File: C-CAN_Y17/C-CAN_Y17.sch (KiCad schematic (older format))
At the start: 18 parts, among them P1 CAN_Connector, P2 Sensor_Connector, P3 CAN_Terminate, SW1 SW_Push, U1 MCP2551-I/SN, U2 AP111750, U3 Cypress_5LP, Y1 Crystal

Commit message: Remove uneccesary junctions, add MX150 symbols
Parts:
- removed R2: 1k, Resistors_SMD:R_0805_HandSoldering, symbol R
- added P?: MX150_16, symbol MX150_16
- added P?: MX150_8, symbol MX150_8
- added R2: 1k, symbol R_Small
- P1: symbol CONN_02X04 -> CONN_02X04-RESCUE-C-CAN_Y17
- P2: symbol CONN_02X08 -> CONN_02X08-RESCUE-C-CAN_Y17
- U2: symbol AP111750 -> AP111750-RESCUE-C-CAN_Y17
- Y1: symbol Crystal -> Crystal-RESCUE-C-CAN_Y17
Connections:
- net +12V: now also P?.1 (P1), P?.4 (P7)
- net +5V: now also P?.1 (P1), P?.12, P?.4, P?.7, P?.9, R2.2
- net GND: now also P?.11, P?.14, P?.15, P?.16, P?.3, P?.5 (P2), P?.6, P?.8 (P8)
- net H1: now also P?.8
- net S1: now also P?.2
- net S2: now also P?.5
- net S3: now also P?.10
- net S4: now also P?.13
- net at SW1.1, U3.24 (RESET): now also R2.1
- new net CANH: P?.2 (P3), P?.3 (P5)
- new net CANL: P?.6 (P4), P?.7 (P6)

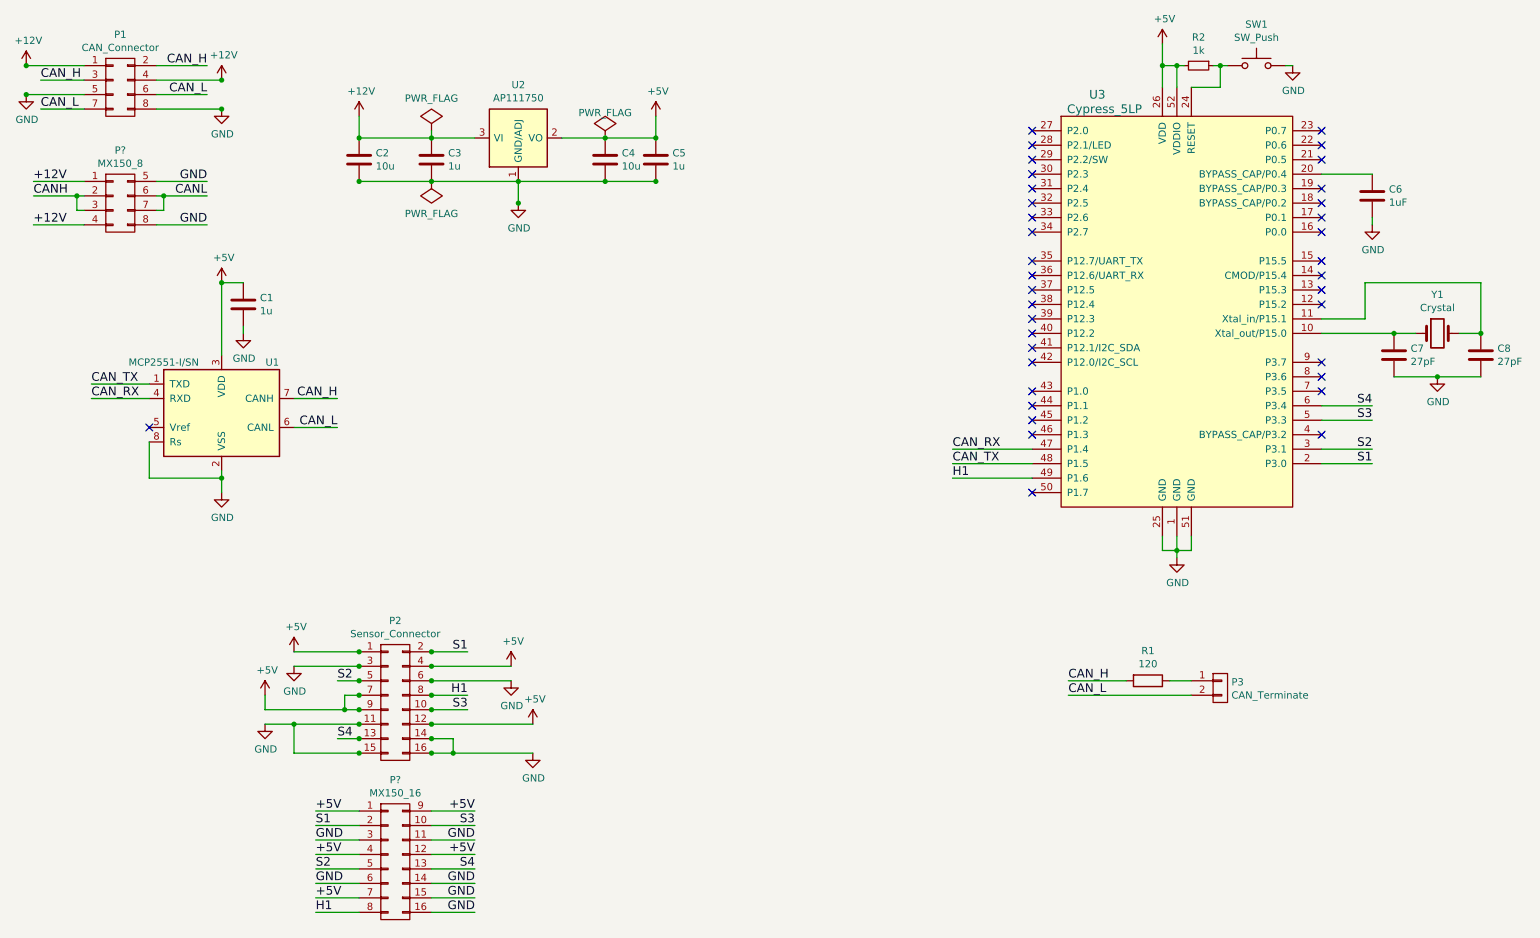
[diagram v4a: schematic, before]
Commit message: Fix AP1117 error, remove extraneous PWR_FLAG
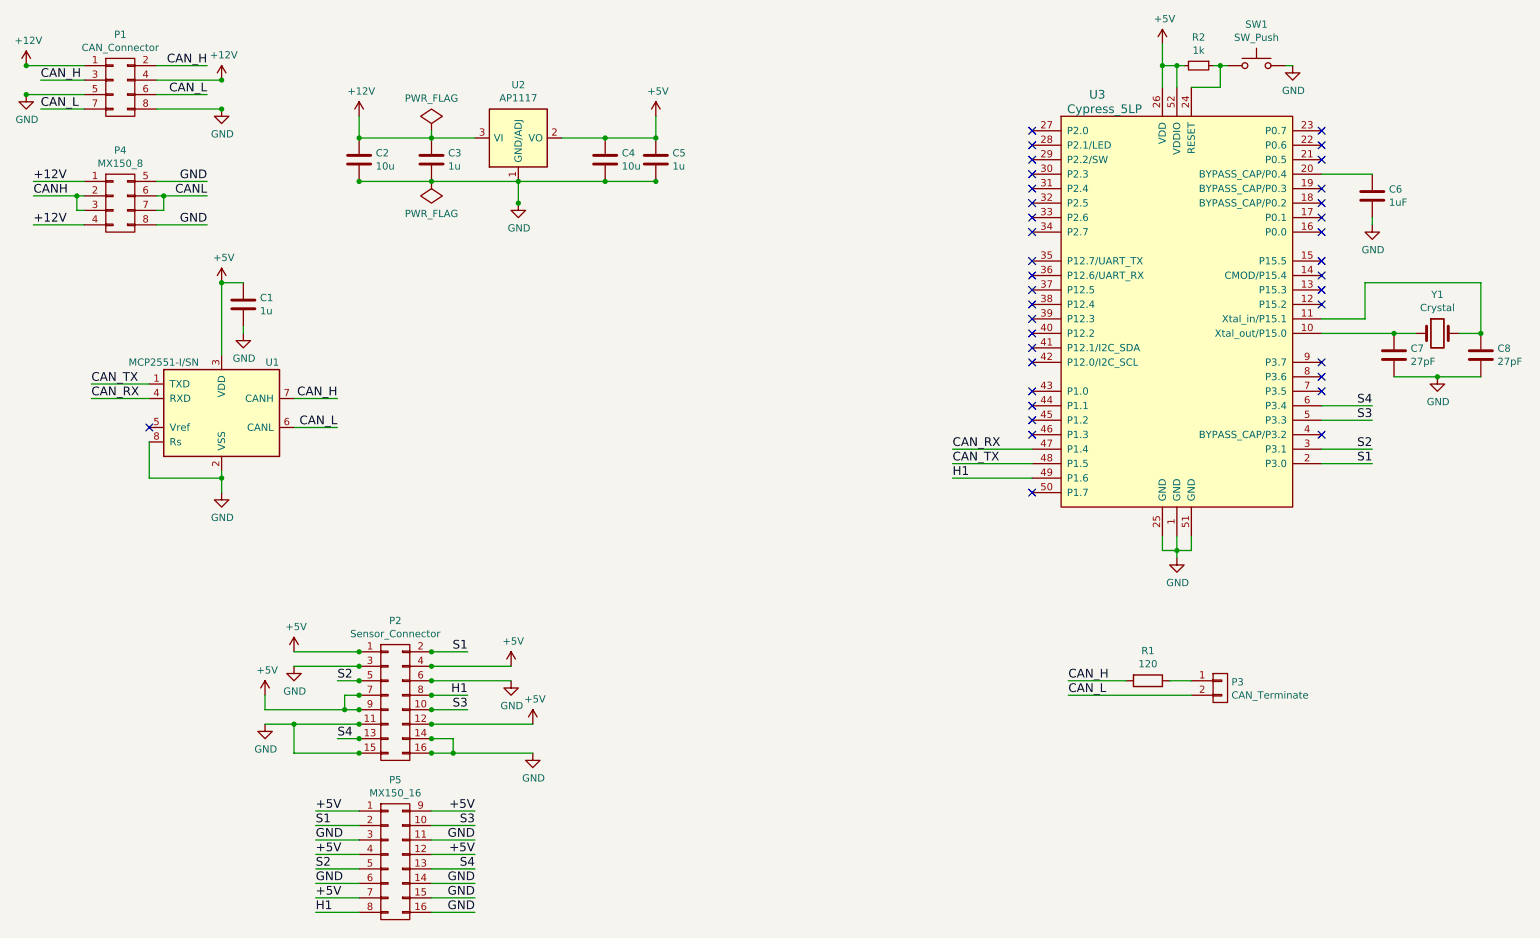
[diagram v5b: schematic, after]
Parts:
- removed U2: AP111750, TO_SOT_Packages_SMD:SOT-223, symbol AP111750-RESCUE-C-CAN_Y17
- added U2: AP1117, TO_SOT_Packages_SMD:SOT-223, symbol AP1117
- gave numbers to parts that had none: 2
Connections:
- net +12V: now also U2.3 (VI)
- net +5V: now also U2.2 (VO), U2.4 (VO)
- net GND: now also U2.1 (GND/ADJ)
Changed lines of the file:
@@
 EESchema Schematic File Version 2
+LIBS:UNCAMotorsports
 LIBS:C-CAN_Y17-rescue
-LIBS:UNCAMotorsports
 LIBS:power
 LIBS:device
@@
 $EndComp
 $Comp
-L +12V #PWR12
+L +12V #PWR01
 U 1 1 58B77F9E
 P 3150 1300
-F 0 "#PWR12" H 3150 1150 50  0001 C CNN
+F 0 "#PWR01" H 3150 1150 50  0001 C CNN
 F 1 "+12V" H 3165 1473 50  0000 C CNN
 F 2 "" H 3150 1300 50  0000 C CNN
@@
 $EndComp
 $Comp
-L +5V #PWR18
+L +5V #PWR02
 U 1 1 58B77FBC
 P 5200 1300
-F 0 "#PWR18" H 5200 1150 50  0001 C CNN
+F 0 "#PWR02" H 5200 1150 50  0001 C CNN
 F 1 "+5V" H 5215 1473 50  0000 C CNN
 F 2 "" H 5200 1300 50  0000 C CNN
@@
 	5200 1450 5200 1300
 $Comp
-L GND #PWR15
+L GND #PWR03
 U 1 1 58B78147
 P 4250 1900
-F 0 "#PWR15" H 4250 1650 50  0001 C CNN
+F 0 "#PWR03" H 4250 1650 50  0001 C CNN
 F 1 "GND" H 4255 1727 50  0000 C CNN
 F 2 "" H 4250 1900 50  0000 C CNN
@@
 Connection ~ 4850 1750
 $Comp
-L GND #PWR6
+L GND #PWR04
 U 1 1 58B78482
 P 2200 3900
-F 0 "#PWR6" H 2200 3650 50  0001 C CNN
+F 0 "#PWR04" H 2200 3650 50  0001 C CNN
 F 1 "GND" H 2205 3727 50  0000 C CNN
 F 2 "" H 2200 3900 50  0000 C CNN
@@
 	2700 3450 3000 3450
 $Comp
-L +5V #PWR5
+L +5V #PWR05
 U 1 1 58B786DB
 P 2200 2450
-F 0 "#PWR5" H 2200 2300 50  0001 C CNN
+F 0 "#PWR05" H 2200 2300 50  0001 C CNN
 F 1 "+5V" H 2215 2623 50  0000 C CNN
 F 2 "" H 2200 2450 50  0000 C CNN
@@
 $EndComp
 $Comp
-L GND #PWR7
+L GND #PWR06
 U 1 1 58B7879B
 P 2350 2800
-F 0 "#PWR7" H 2350 2550 50  0001 C CNN
+F 0 "#PWR06" H 2350 2550 50  0001 C CNN
 F 1 "GND" H 2355 2627 50  0000 C CNN
 F 2 "" H 2350 2800 50  0000 C CNN
@@
 	2100 950  1750 950
 $Comp
-L +12V #PWR1
+L +12V #PWR07
 U 1 1 58B7A343
 P 850 950
-F 0 "#PWR1" H 850 800 50  0001 C CNN
+F 0 "#PWR07" H 850 800 50  0001 C CNN
 F 1 "+12V" H 865 1123 50  0000 C CNN
 F 2 "" H 850 950 50  0000 C CNN
@@
 	850  950  1250 950
 $Comp
-L +12V #PWR3
+L +12V #PWR08
 U 1 1 58B7A390
 P 2200 1050
-F 0 "#PWR3" H 2200 900 50  0001 C CNN
+F 0 "#PWR08" H 2200 900 50  0001 C CNN
 F 1 "+12V" H 2215 1223 50  0000 C CNN
 F 2 "" H 2200 1050 50  0000 C CNN
@@
 	2200 1050 1750 1050
 $Comp
-L GND #PWR2
+L GND #PWR09
 U 1 1 58B7A3DE
 P 850 1150
-F 0 "#PWR2" H 850 900 50  0001 C CNN
+F 0 "#PWR09" H 850 900 50  0001 C CNN
 F 1 "GND" H 855 977 50  0000 C CNN
 F 2 "" H 850 1150 50  0000 C CNN
@@
 	850  1150 1250 1150
 $Comp
-L GND #PWR4
+L GND #PWR010
 U 1 1 58B7A438
 P 2200 1250
-F 0 "#PWR4" H 2200 1000 50  0001 C CNN
+F 0 "#PWR010" H 2200 1000 50  0001 C CNN
 F 1 "GND" H 2205 1077 50  0000 C CNN
 F 2 "" H 2200 1250 50  0000 C CNN
@@
 	950  1050 1250 1050
 $Comp
-L +5V #PWR10
+L +5V #PWR011
 U 1 1 58B7AF23
 P 2700 5000
-F 0 "#PWR10" H 2700 4850 50  0001 C CNN
+F 0 "#PWR011" H 2700 4850 50  0001 C CNN
 F 1 "+5V" H 2715 5173 50  0000 C CNN
 F 2 "" H 2700 5000 50  0000 C CNN
@@
 	3900 5000 3650 5000
 $Comp
-L GND #PWR11
+L GND #PWR012
 U 1 1 58B7B062
 P 2700 5100
-F 0 "#PWR11" H 2700 4850 50  0001 C CNN
+F 0 "#PWR012" H 2700 4850 50  0001 C CNN
 F 1 "GND" H 2705 4927 50  0000 C CNN
 F 2 "" H 2700 5100 50  0000 C CNN
@@
 	2700 5100 3150 5100
 $Comp
-L +5V #PWR13
+L +5V #PWR013
 U 1 1 58B7B0B7
 P 4200 5100
-F 0 "#PWR13" H 4200 4950 50  0001 C CNN
+F 0 "#PWR013" H 4200 4950 50  0001 C CNN
 F 1 "+5V" H 4215 5273 50  0000 C CNN
 F 2 "" H 4200 5100 50  0000 C CNN
@@
 	3000 5200 3150 5200
 $Comp
-L GND #PWR14
+L GND #PWR014
 U 1 1 58B7B15B
 P 4200 5200
-F 0 "#PWR14" H 4200 4950 50  0001 C CNN
+F 0 "#PWR014" H 4200 4950 50  0001 C CNN
 F 1 "GND" H 4205 5027 50  0000 C CNN
 F 2 "" H 4200 5200 50  0000 C CNN
@@
 	4200 5200 3650 5200
 $Comp
-L +5V #PWR8
+L +5V #PWR015
 U 1 1 58B7B1B3
 P 2500 5300
-F 0 "#PWR8" H 2500 5150 50  0001 C CNN
+F 0 "#PWR015" H 2500 5150 50  0001 C CNN
 F 1 "+5V" H 2515 5473 50  0000 C CNN
 F 2 "" H 2500 5300 50  0000 C CNN
@@
 	3900 5400 3650 5400
 $Comp
-L GND #PWR9
+L GND #PWR016
 U 1 1 58B9FCC5
 P 2500 5500
-F 0 "#PWR9" H 2500 5250 50  0001 C CNN
+F 0 "#PWR016" H 2500 5250 50  0001 C CNN
 F 1 "GND" H 2505 5327 50  0000 C CNN
 F 2 "" H 2500 5500 50  0000 C CNN
@@
 	2500 5500 3150 5500
 $Comp
-L +5V #PWR16
+L +5V #PWR017
 U 1 1 58B9FD2F
 P 4350 5500
-F 0 "#PWR16" H 4350 5350 50  0001 C CNN
+F 0 "#PWR017" H 4350 5350 50  0001 C CNN
 F 1 "+5V" H 4365 5673 50  0000 C CNN
 F 2 "" H 4350 5500 50  0000 C CNN
@@
 Connection ~ 2700 5500
 $Comp
-L GND #PWR17
+L GND #PWR018
 U 1 1 58B9FEC2
 P 4350 5700
-F 0 "#PWR17" H 4350 5450 50  0001 C CNN
+F 0 "#PWR018" H 4350 5450 50  0001 C CNN
 F 1 "GND" H 4355 5527 50  0000 C CNN
 F 2 "" H 4350 5700 50  0000 C CNN
@@
 	7250 3700 7800 3700
 $Comp
-L GND #PWR20
+L GND #PWR019
 U 1 1 58BA0B14
 P 8800 4350
-F 0 "#PWR20" H 8800 4100 50  0001 C CNN
+F 0 "#PWR019" H 8800 4100 50  0001 C CNN
 F 1 "GND" H 8805 4177 50  0000 C CNN
 F 2 "" H 8800 4350 50  0000 C CNN
@@
 	8700 4300 8700 4200
 $Comp
-L +5V #PWR19
+L +5V #PWR020
 U 1 1 58BA0DD0
 P 8700 800
-F 0 "#PWR19" H 8700 650 50  0001 C CNN
+F 0 "#PWR020" H 8700 650 50  0001 C CNN
 F 1 "+5V" H 8715 973 50  0000 C CNN
 F 2 "" H 8700 800 50  0000 C CNN
@@
 $EndComp
 $Comp
-L GND #PWR21
+L GND #PWR021
 U 1 1 58BA0480
 P 9600 950
-F 0 "#PWR21" H 9600 700 50  0001 C CNN
+F 0 "#PWR021" H 9600 700 50  0001 C CNN
 F 1 "GND" H 9605 777 50  0000 C CNN
 F 2 "" H 9600 950 50  0000 C CNN
@@
 	10300 3100 10900 3100
 $Comp
-L GND #PWR23
+L GND #PWR022
 U 1 1 58BA0CB8
 P 10600 3100
-F 0 "#PWR23" H 10600 2850 50  0001 C CNN
+F 0 "#PWR022" H 10600 2850 50  0001 C CNN
 F 1 "GND" H 10605 2927 50  0000 C CNN
 F 2 "" H 10600 3100 50  0000 C CNN
@@
 	10150 1700 9800 1700
 $Comp
-L GND #PWR22
+L GND #PWR023
 U 1 1 58BA1105
 P 10150 2050
-F 0 "#PWR22" H 10150 1800 50  0001 C CNN
+F 0 "#PWR023" H 10150 1800 50  0001 C CNN
 F 1 "GND" H 10155 1877 50  0000 C CNN
 F 2 "" H 10150 2050 50  0000 C CNN
@@
 NoConn ~ 9800 3500
 $Comp
-L PWR_FLAG #FLG1
+L PWR_FLAG #FLG024
 U 1 1 58BA2BC0
 P 3650 1400
-F 0 "#FLG1" H 3650 1495 50  0001 C CNN
+F 0 "#FLG024" H 3650 1495 50  0001 C CNN
 F 1 "PWR_FLAG" H 3650 1624 50  0000 C CNN
 F 2 "" H 3650 1400 50  0000 C CNN
@@
 $EndComp
 $Comp
-L PWR_FLAG #FLG2
+L PWR_FLAG #FLG025
 U 1 1 58BA2BF8
 P 3650 1750
-F 0 "#FLG2" H 3650 1845 50  0001 C CNN
+F 0 "#FLG025" H 3650 1845 50  0001 C CNN
 F 1 "PWR_FLAG" H 3650 1973 50  0000 C CNN
 F 2 "" H 3650 1750 50  0000 C CNN
@@
 	1    3650 1750
 	-1   0    0    1
-$EndComp
-$Comp
-L AP111750-RESCUE-C-CAN_Y17 U2
-U 1 1 58BA14E8
-P 4250 1450
-F 0 "U2" H 4250 1817 50  0000 C CNN
-F 1 "AP111750" H 4250 1726 50  0000 C CNN
-F 2 "TO_SOT_Packages_SMD:SOT-223" H -100 -200 50  0001 C CNN
-F 3 "" H 0   -100 50  0001 C CNN
-	1    4250 1450
-	1    0    0    -1
 $EndComp
 Wire Wire Line
@@
 Connection ~ 3650 5700
 $Comp
-L PWR_FLAG #FLG3
-U 1 1 58BA3F4D
-P 4850 1450
-F 0 "#FLG3" H 0   125 50  0001 C CNN
-F 1 "PWR_FLAG" H 4850 1624 50  0000 C CNN
-F 2 "" H 0   50  50  0001 C CNN
-F 3 "" H 0   50  50  0001 C CNN
-	1    4850 1450
-	1    0    0    -1
-$EndComp
-$Comp
 L Cypress_5LP U3
 U 1 1 58B77315
@@
 	3650 1450 3650 1400
 $Comp
-L MX150_16 P?
+L MX150_16 P5
 U 1 1 58BD2E1F
 P 3400 6450
-F 0 "P?" H 3400 7015 50  0000 C CNN
+F 0 "P5" H 3400 7015 50  0000 C CNN
 F 1 "MX150_16" H 3400 6924 50  0000 C CNN
 F 2 "" H -2050 0   50  0000 C CNN
@@
 GND
 $Comp
-L MX150_8 P?
+L MX150_8 P4
 U 1 1 58BD5DFF
 P 1500 1900
-F 0 "P?" H 1500 2265 50  0000 C CNN
+F 0 "P4" H 1500 2265 50  0000 C CNN
 F 1 "MX150_8" H 1500 2174 50  0000 C CNN
 F 2 "" H 150 -850 50  0000 C CNN
@@
 Text Label 2100 2050 2    60   ~ 0
 GND
+$Comp
+L AP1117 U2
+U 1 1 58BD7651
+P 4250 1450
+F 0 "U2" H 4250 1817 50  0000 C CNN
+F 1 "AP1117" H 4250 1726 50  0000 C CNN
+F 2 "TO_SOT_Packages_SMD:SOT-223" H 0   -350 50  0001 C CNN
+F 3 "" H 100 -250 50  0001 C CNN
+	1    4250 1450
+	1    0    0    -1
+$EndComp
 $EndSCHEMATC

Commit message: C-CAN layout done. Needs to be compared to oshpark DRC still.
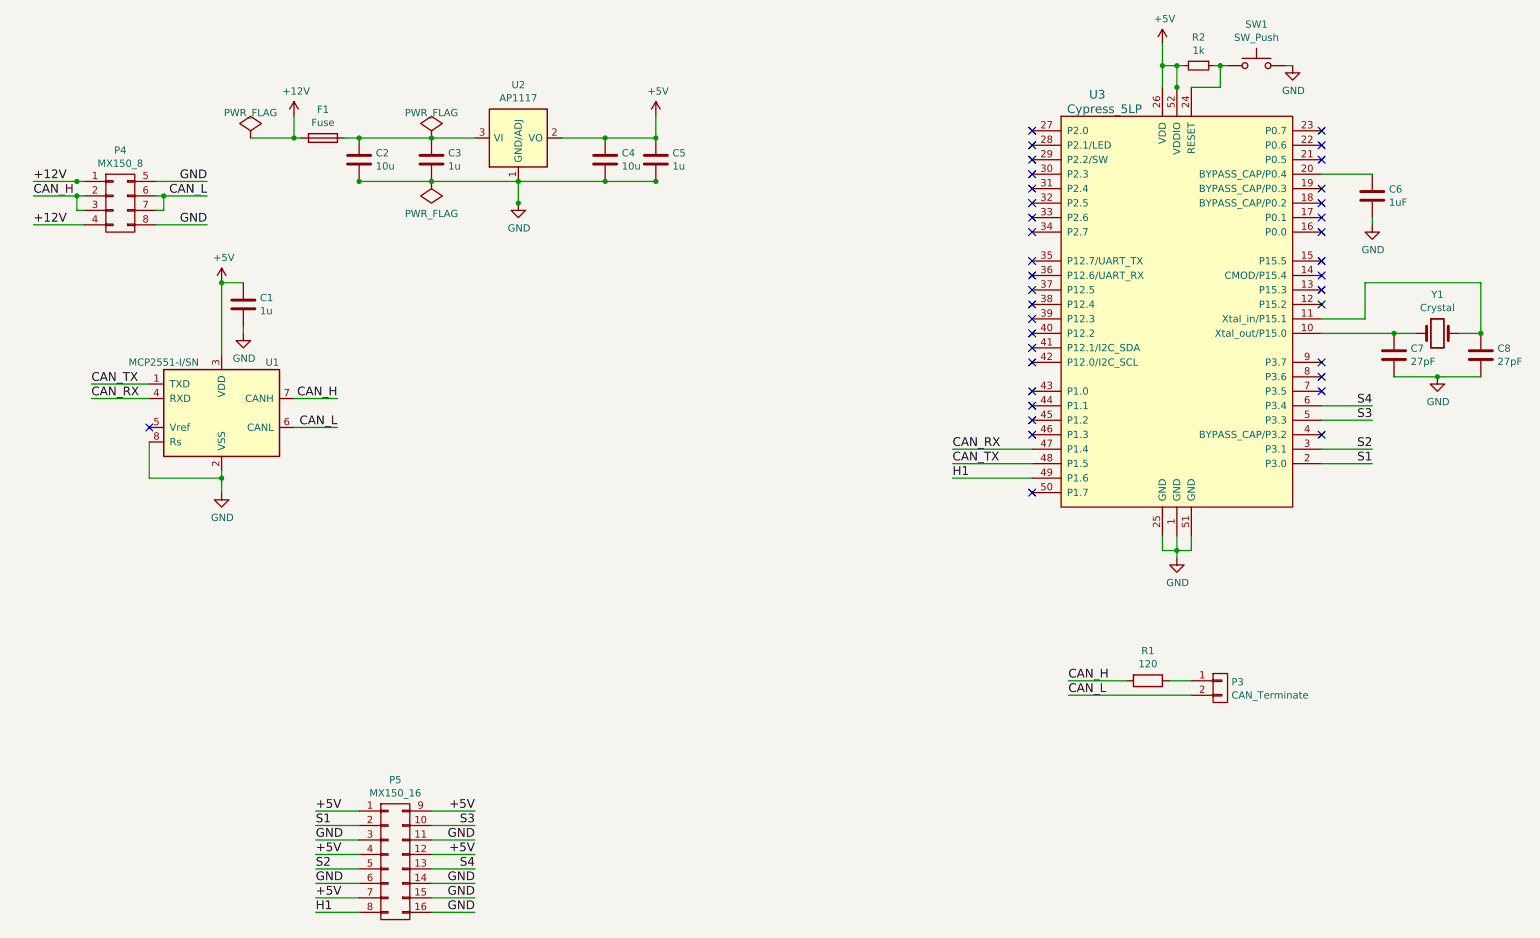
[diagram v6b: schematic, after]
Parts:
- removed P1: CAN_Connector, UNCAMotorsports:MX150_8Pin, symbol CONN_02X04-RESCUE-C-CAN_Y17
- removed P2: Sensor_Connector, UNCAMotorsports:MX150_16pin, symbol CONN_02X08-RESCUE-C-CAN_Y17
- added F1: Fuse, Fuse_Holders_and_Fuses:Fuse_SMD1206_HandSoldering, symbol Fuse
- P4: footprint (none) -> UNCAMotorsports:MX150_8Pin
- P5: footprint (none) -> UNCAMotorsports:MX150_16pin
- R2: footprint (none) -> Resistors_SMD:R_0805_HandSoldering
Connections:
- net CANH is gone; now on net CAN_H: P4.2 (P3), P4.3 (P5)
- net CANL is gone; now on net CAN_L: P4.6 (P4), P4.7 (P6)
- net +12V: now also F1.2; no longer C2.1, C3.1, U2.3 (VI)
- new net: C2.1, C3.1, F1.1, U2.3 (VI)
